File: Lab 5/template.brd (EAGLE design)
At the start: 100 x 80 mm, 48 parts, among them J1 FTDI_DEVICERA_SMT, M1 WIRELESS-NRF24L01, U1 3.3V, U2 GY-521MPU6050

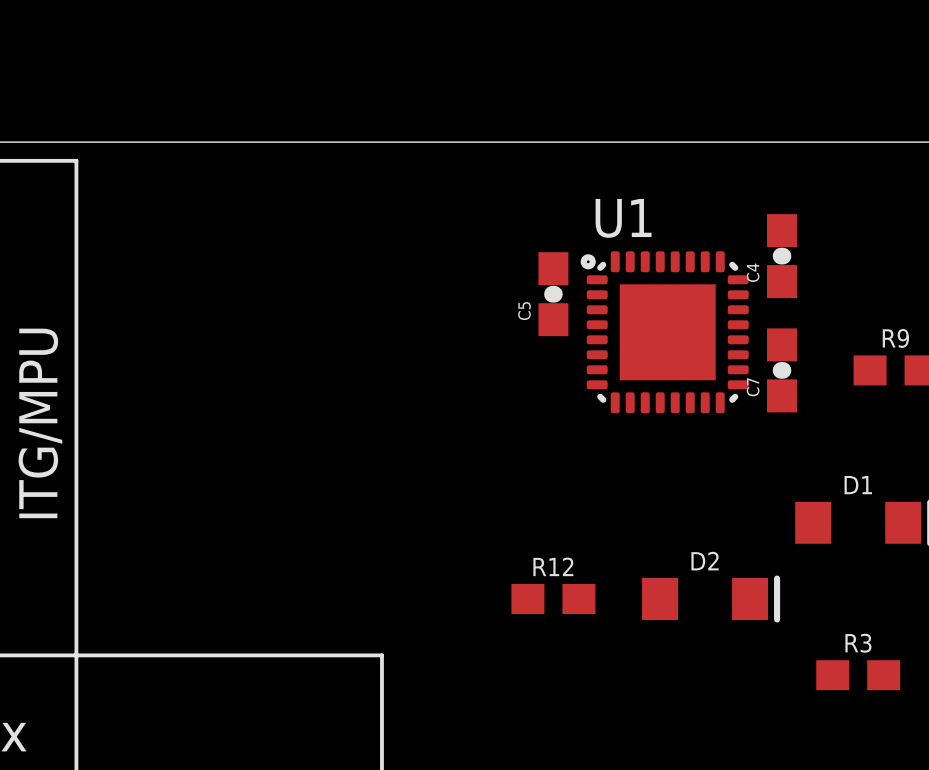
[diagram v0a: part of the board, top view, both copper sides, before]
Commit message: Update template file, switch for the right Atmega MCU. Some advice from Arti:   - Everything need to be inside the board (all white frames inside): quadcopter propellers need clearance.   - Nothing under white frame except the Radio Module   - Battery JBT need to have +- on the edge of the PCB   - Mandatory: Top Polygon: VCC, Bottom Polygon: GND; Don't worry about Digital and Analog VCC and GND.
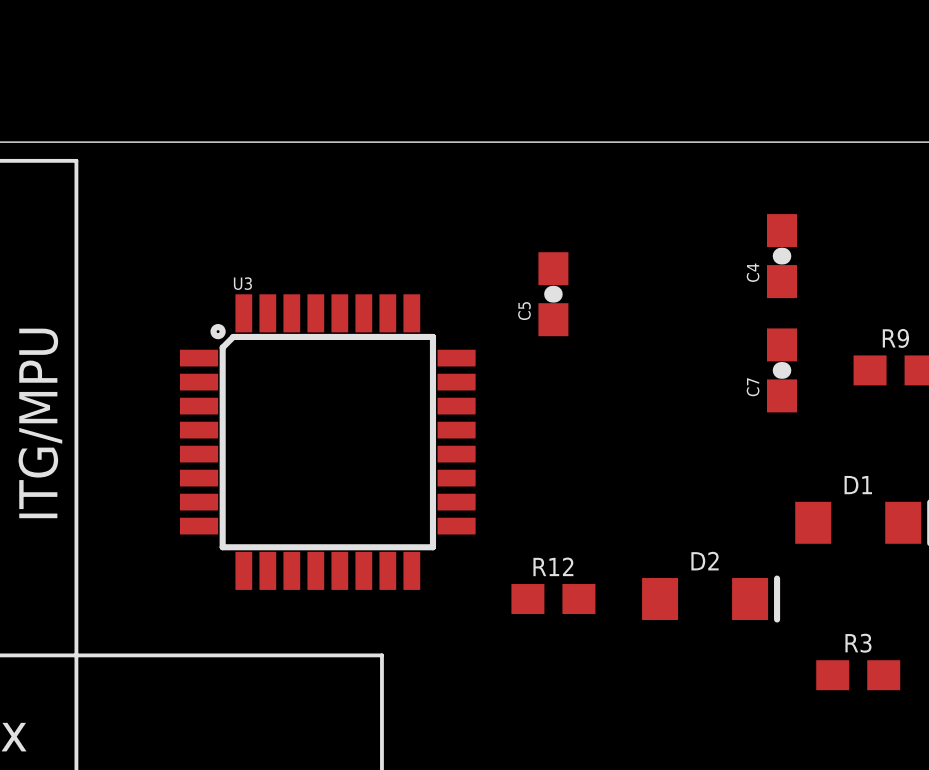
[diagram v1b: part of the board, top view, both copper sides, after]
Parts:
- removed U1: 3.3V, SparkFun-DigitalIC:MLF32-PAD
- added U3: ATMEGA328P_TQFP, quad:TQFP32-08
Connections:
- removed net N$3 (its old number): R9.2, U1.27
- new net N$8: R9.2, U3.27
- net FTDI-RX: now also U3.30; no longer U1.30
- net FTDI-TX: now also U3.31; no longer U1.31
- net GND: now also U3.21, U3.3, U3.5; no longer U1.21, U1.3, U1.5, U1.PAD
- net IMU-INT: now also U3.1; no longer U1.1
- net MEASURE_PIN: now also U3.2; no longer U1.2
- net MOTOR1: now also U3.32; no longer U1.32
- net MOTOR2: now also U3.9; no longer U1.9
- net MOTOR3: now also U3.10; no longer U1.10
- net MOTOR4: now also U3.13; no longer U1.13
- net N$10: now also U3.28; no longer U1.28
- net N$2: now also U3.20; no longer U1.20
- net OSC1: now also U3.7; no longer U1.7
- net RESET: now also U3.29; no longer U1.29
- net RF-CE: now also U3.12; no longer U1.12
- net RF-CSN: now also U3.14; no longer U1.14
- net RF-MISO: now also U3.16; no longer U1.16
- net RF-MOSI: now also U3.15; no longer U1.15
- net RF-SCK: now also U3.17; no longer U1.17
- net VCC: now also U3.18, U3.4; no longer U1.18, U1.4
